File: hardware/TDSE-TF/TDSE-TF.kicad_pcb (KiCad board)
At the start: 2 copper layers, 153.2 x 91.6 mm, 37 parts, among them J1 Nivel de agua, J10 CN10, J2 Tira LED, J3 +5VCC entrada, J5 Bomba, J6 Nivel de luz, J7 CN7, J8 Humedad de suelo, J9 Conector LCD16x02, Q1 IRLZ44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

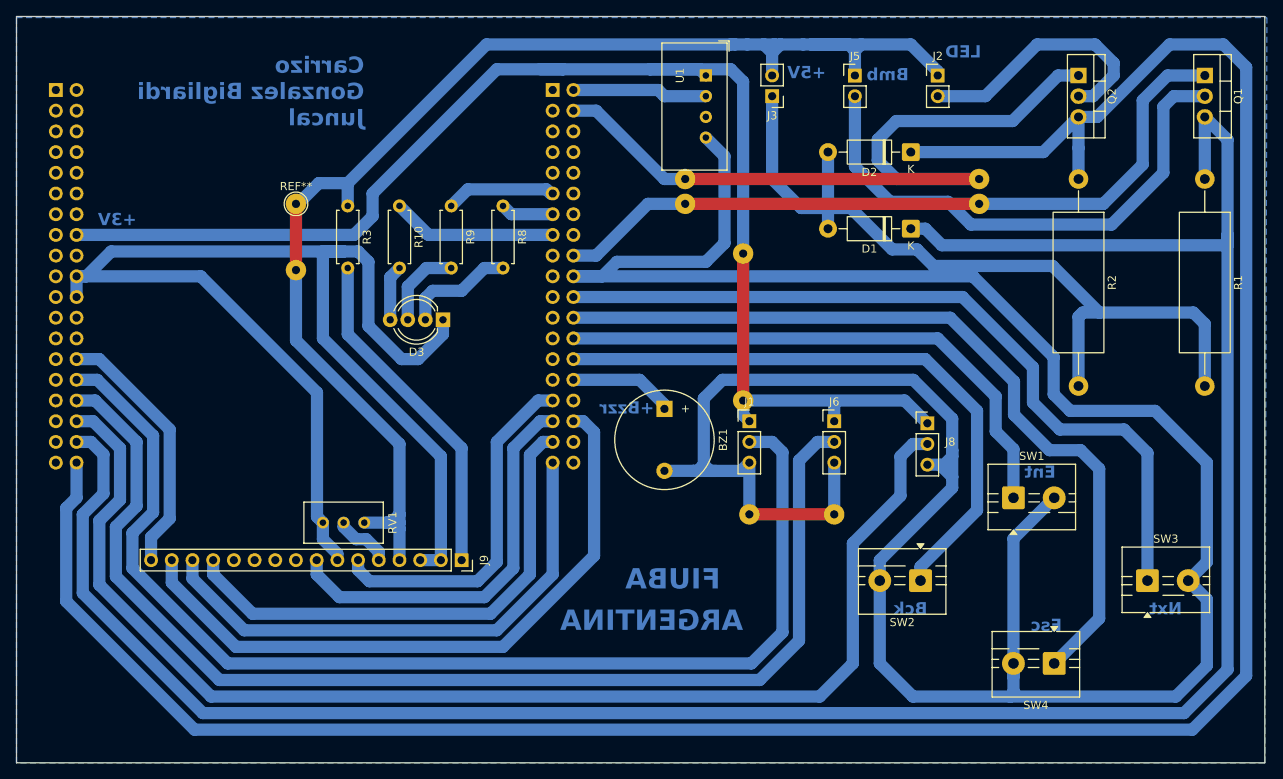
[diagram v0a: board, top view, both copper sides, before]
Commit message: Circuito final - Rev2
Revisión 2 del circuito esquemático y del PCB.
Cambios en conexiones del LCD.
Ajustes de Capa FFab.
Adjunto nota sobre configuración de jumpres y orden de conexionado de la placa.
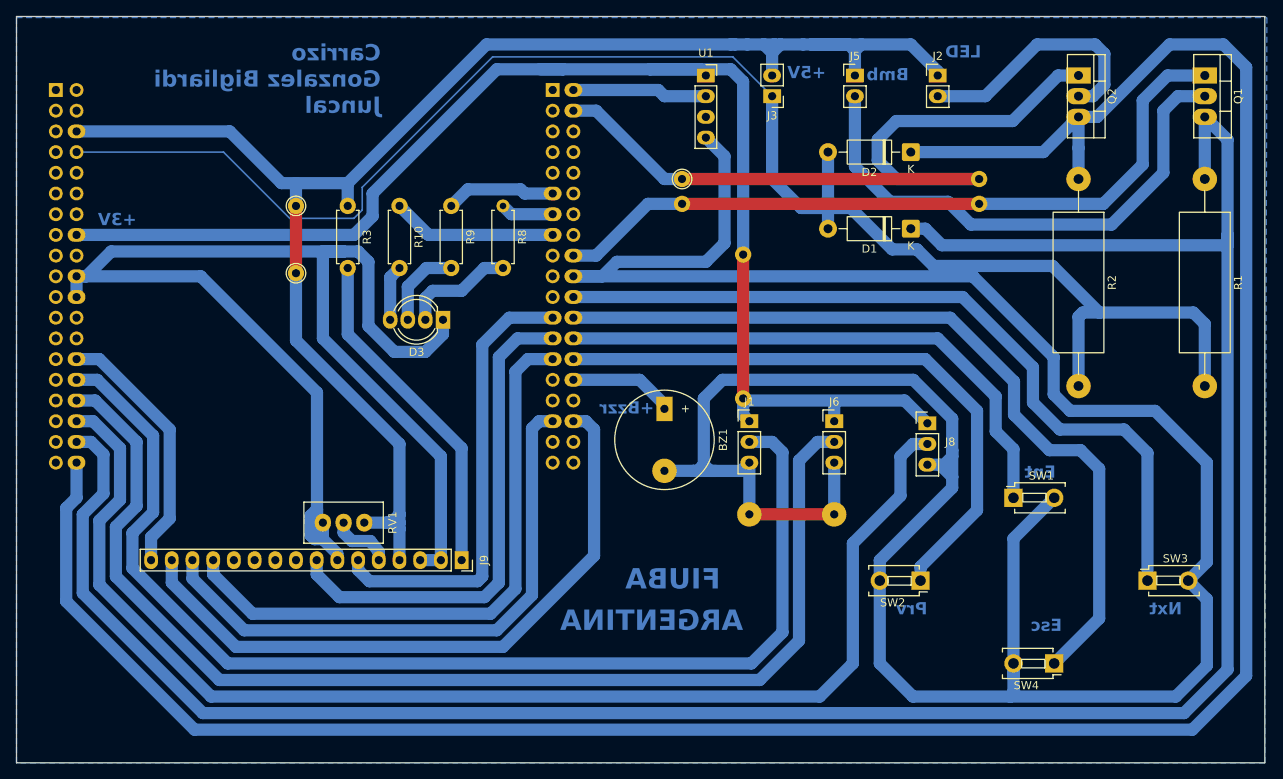
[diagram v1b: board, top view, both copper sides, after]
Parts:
- removed the ? at (212.6, 61.0)
- removed the ? at (212.6, 42.9)
- removed the ? at (205.5, 36.8)
- removed the ? at (157.7, 45.0)
- removed the ? at (205.5, 33.8)
- removed the REF** at (157.7, 36.8)
- added ?: , , F.Cu at (205.1, 36.8)
- added ?: , , F.Cu at (212.6, 43.1)
- added ?: , , F.Cu at (212.6, 60.7)
- added REF**: TestPoint_THTPad_D2.0mm_Drill1.0mm, TestPoint:TestPoint_THTPad_D2.0mm_Drill1.0mm, F.Cu at (157.7, 37.1)
- added REF**: TestPoint_THTPad_D2.0mm_Drill1.0mm, TestPoint:TestPoint_THTPad_D2.0mm_Drill1.0mm, F.Cu at (157.7, 45.3)
- added REF**: TestPoint_THTPad_D2.0mm_Drill1.0mm, TestPoint:TestPoint_THTPad_D2.0mm_Drill1.0mm, F.Cu at (205.1, 33.8)
- R1: value 10R 2W -> 10 2W
- SW1, SW2, SW3, SW4: footprint TerminalBlock:TerminalBlock_MaiXu_MX126-5.0-02P_1x02_P5.00mm -> Button_Switch_THT:SW_PUSH_1P1T 2 pines
- U1: footprint Sensor:ASAIR_AM2302_P2.54mm_Vertical -> Connector_PinSocket_2.54mm:PinSocket_1x04_P2.54mm_Vertical
- turned U1 to 0 degrees
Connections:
- net /D6 renamed /LCD_D6
- net /D7 renamed /LCD_D7
- J10 pad 23: unconnected-(J10-Pin_23-Pad23) -> /LCD_RS
- J10 pad 25: unconnected-(J10-Pin_25-Pad25) -> /LCD_E
- J10 pad 27: unconnected-(J10-Pin_27-Pad27) -> /LCD_D4
- J10 pad 31: /RS -> unconnected-(J10-Pin_31-Pad31)
- J10 pad 33: /E -> /LCD_D5
- J10 pad 35: /D4 -> unconnected-(J10-Pin_35-Pad35)
- J10 pad 37: /D5 -> unconnected-(J10-Pin_37-Pad37)
- J7 pad 6: unconnected-(J7-Pin_6-Pad6) -> VCC
- J9 pad 13: /D4 -> /LCD_D4
- J9 pad 14: /D5 -> /LCD_D5
- J9 pad 6: /RS -> /LCD_RS
- J9 pad 8: /E -> /LCD_E
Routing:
- net GND: track 607.5 -> 716.5 mm
- net /LCD_D4: track 0.00 -> 74.0 mm
- net /LCD_D5: track 0.00 -> 71.7 mm
- net /D5: track 65.6 -> 0.00 mm
- net /D4: track 62.7 -> 0.00 mm
- net /LCD_E: track 0.00 -> 60.8 mm
- net /LCD_RS: track 0.00 -> 55.7 mm
- net /E: track 49.0 -> 0.00 mm
- net /RS: track 43.5 -> 0.00 mm
- net VCC: track 165.0 -> 196.2 mm
- net Net-(J2-Pin_2): track 32.1 -> 31.1 mm
- net Net-(J9-Pin_5): track 7.12 -> 7.64 mm
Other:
- board text added: "+3,3"
- board text added: "DATA"
- board text added: "Prv"
- board text removed: "Bck"

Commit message: PCB final Rev 2
Corregido conexionado de LCD.
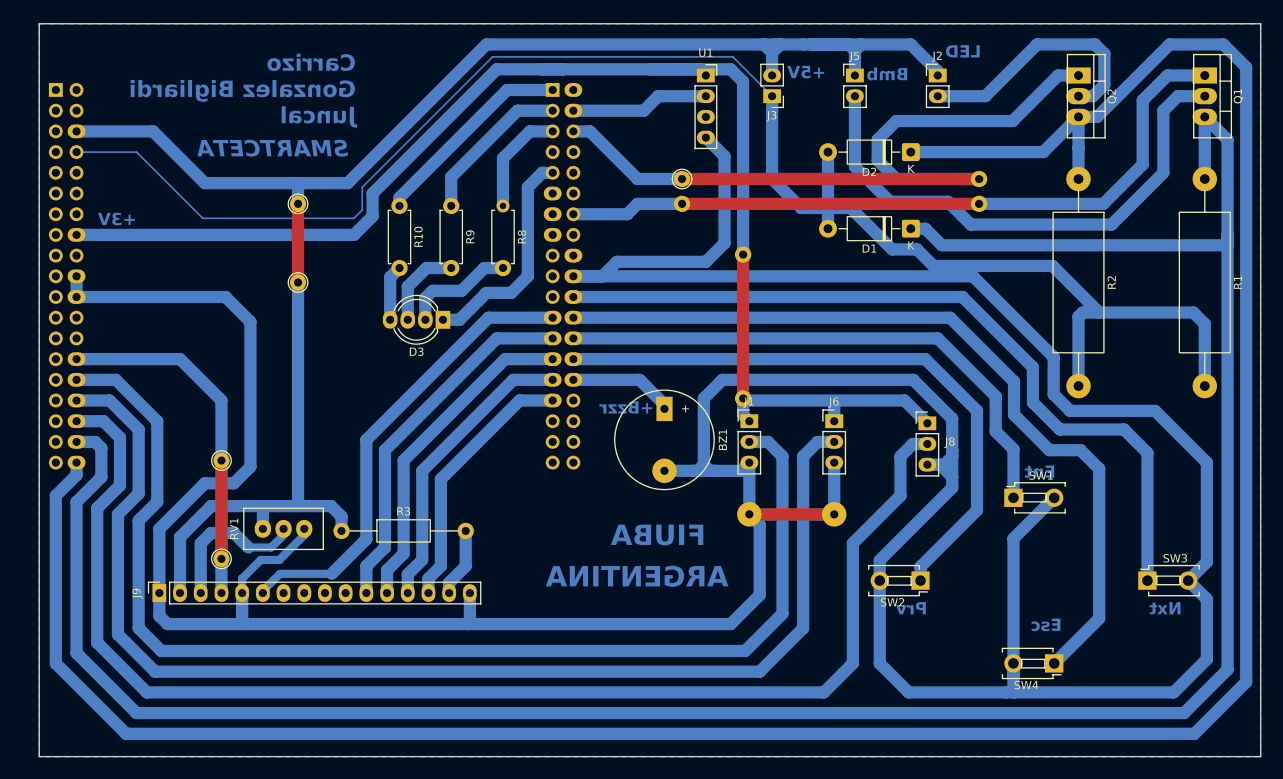
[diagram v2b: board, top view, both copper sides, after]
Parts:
- added REF**: TestPoint_THTPad_D2.0mm_Drill1.0mm, TestPoint:TestPoint_THTPad_D2.0mm_Drill1.0mm, F.Cu at (158.0, 36.8)
- added REF**: TestPoint_THTPad_D2.0mm_Drill1.0mm, TestPoint:TestPoint_THTPad_D2.0mm_Drill1.0mm, F.Cu at (158.0, 46.5)
- J1: value Nivel de agua -> Sensor nivel de agua
- J6: value Nivel de luz -> Sensor nivel de luz
- J8: value Humedad de suelo -> Sensor humedad de suelo
- R3: footprint Resistor_THT:R_Axial_DIN0207_L6.3mm_D2.5mm_P7.62mm_Horizontal -> Resistor_THT:R_Axial_DIN0207_L6.3mm_D2.5mm_P15.24mm_Horizontal
- U1: value DHT22 -> AM2302
- moved R3 39.9 mm to (163.3, 77.0), turned to 0 degrees
- moved J9 37.3 mm to (141.0, 84.6), turned to 90 degrees
- moved REF** 36.2 mm to (148.6, 80.4)
- moved REF** 32.6 mm to (148.6, 68.3), turned to 90 degrees
- moved RV1 12.5 mm to (153.7, 76.7), turned to 90 degrees
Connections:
- J10 pad 1: unconnected-(J10-Pin_1-Pad1) -> /LED Azul
- J10 pad 11: /LED Verde -> unconnected-(J10-Pin_11-Pad11)
- J10 pad 13: /LED Rojo -> unconnected-(J10-Pin_13-Pad13)
- J10 pad 14: unconnected-(J10-Pin_14-Pad14) -> /Driver Bomba
- J10 pad 15: /LED Azul -> unconnected-(J10-Pin_15-Pad15)
- J10 pad 18: /Driver Bomba -> unconnected-(J10-Pin_18-Pad18)
- J10 pad 2: /Medicion DHT22 (AM2302) -> unconnected-(J10-Pin_2-Pad2)
- J10 pad 23: /LCD_RS -> /LCD_E
- J10 pad 25: /LCD_E -> /LCD_D4
- J10 pad 27: /LCD_D4 -> /LCD_D5
- J10 pad 29: unconnected-(J10-Pin_29-Pad29) -> /LCD_D6
- J10 pad 3: unconnected-(J10-Pin_3-Pad3) -> /LED Verde
- J10 pad 31: unconnected-(J10-Pin_31-Pad31) -> /LCD_D7
- J10 pad 33: /LCD_D5 -> unconnected-(J10-Pin_33-Pad33)
- J10 pad 34: /LCD_D6 -> unconnected-(J10-Pin_34-Pad34)
- J10 pad 4: /Driver Tira LED -> /Medicion DHT22 (AM2302)
- J10 pad 5: unconnected-(J10-Pin_5-Pad5) -> /LED Rojo
- J10 pad 6: unconnected-(J10-Pin_6-Pad6) -> /Driver Tira LED
- J7 pad 28: /LCD_D7 -> /LCD_RS
- J9 pad 1: Net-(J9-Pin_1) -> GND
- J9 pad 11: unconnected-(J9-Pin_11-Pad11) -> /LCD_D4
- J9 pad 12: unconnected-(J9-Pin_12-Pad12) -> /LCD_D5
- J9 pad 13: /LCD_D4 -> /LCD_D6
- J9 pad 14: /LCD_D5 -> /LCD_D7
- J9 pad 15: /LCD_D6 -> /LCD_A
- J9 pad 16: /LCD_D7 -> GND
- J9 pad 2: GND -> VCC
- J9 pad 3: GND -> /LCD_Vo
- J9 pad 4: VCC -> /LCD_RS
- J9 pad 5: Net-(J9-Pin_5) -> GND
- J9 pad 6: /LCD_RS -> /LCD_E
- J9 pad 7: GND -> unconnected-(J9-Pin_7-Pad7)
- J9 pad 8: /LCD_E -> unconnected-(J9-Pin_8-Pad8)
- R3 pad 2: Net-(J9-Pin_1) -> /LCD_A
- REF** pad 1: VCC -> /LCD_RS
- REF** pad 2: (no net) -> /LCD_RS
- RV1 pad 2: Net-(J9-Pin_5) -> /LCD_Vo
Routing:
- net /LCD_D6: track 80.9 -> 36.4 mm
- net Net-(J9-Pin_1): track 40.8 -> 0.00 mm
- net /LCD_D5: track 71.7 -> 40.5 mm
- net /LCD_D4: track 74.0 -> 44.7 mm
- net GND: track 716.5 -> 739.9 mm
- net /LCD_Vo: track 0.00 -> 18.9 mm
- net /LCD_RS: track 55.7 -> 43.5 mm
- net VCC: track 196.2 -> 206.9 mm
- net /LCD_A: track 0.00 -> 8.46 mm
- net Net-(J9-Pin_5): track 7.64 -> 0.00 mm
- net /Medicion corriente tira LED: track 301.7 -> 308.8 mm
- net /LED Rojo: track 6.52 -> 13.3 mm
- net /LED Verde: track 13.5 -> 19.4 mm
- net /Medicion corriente bomba: track 288.1 -> 293.6 mm
- net /LED Azul: track 20.3 -> 25.3 mm
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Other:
- board size 153.2 x 91.6 mm -> 149.9 x 89.9 mm
- board text added: "0 5 Vo RS 0 E"
- board text added: "B G R"
- board text added: "D4 D5 D6 D7 A K"
- board text added: "SMARTCETA"
- board text removed: "D7 D6 D5 D4"
- board text removed: "E 0 RS Vo 5 0 0 5"

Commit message: PCB final Rev 3
Mejorados detalles del PCB y serigrafía
Añadida opcion de agregar un pullup para el dht22
Modificado el .ioc
Creado task_state_led.h (no terminado)
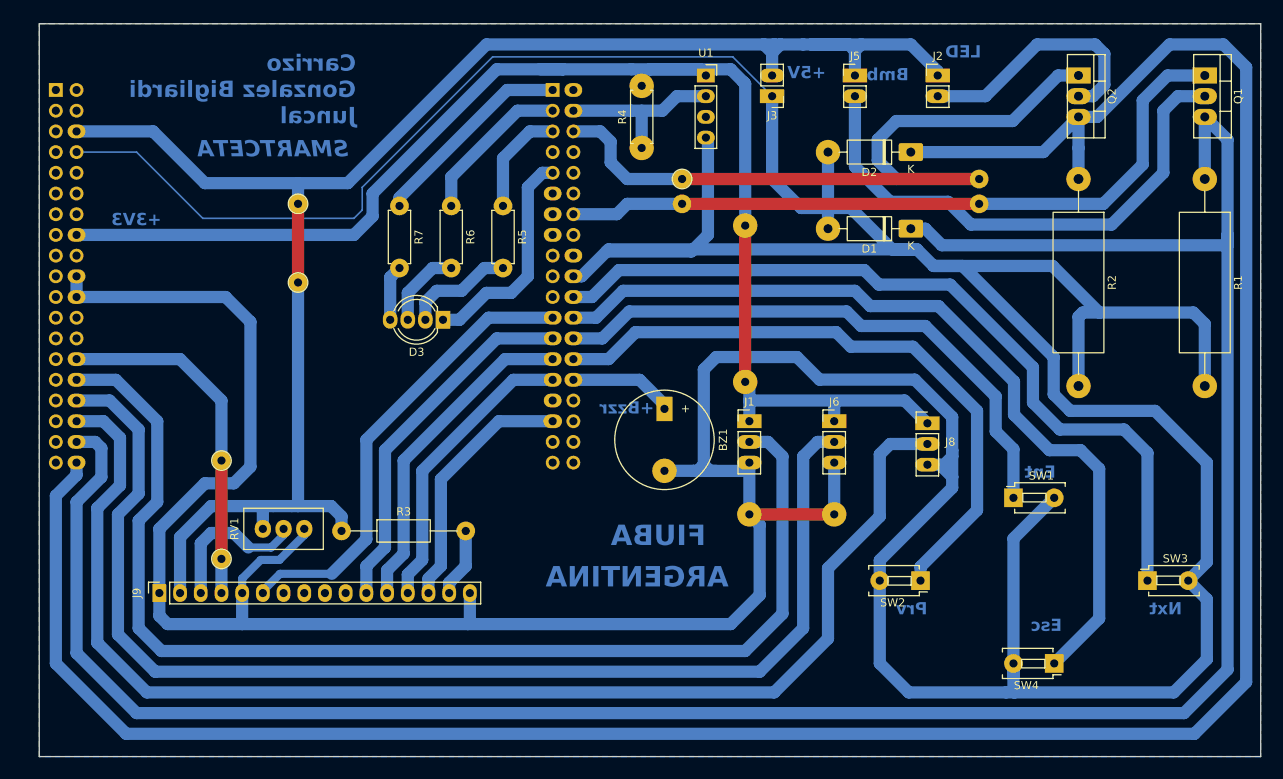
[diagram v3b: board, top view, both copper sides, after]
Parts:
- added R4: 5k1, Resistor_THT:R_Axial_DIN0207_L6.3mm_D2.5mm_P7.62mm_Horizontal, F.Cu at (200.2, 30.0)
- U1: value AM2302 -> DHT22
- moved ? 3.57 mm to (212.9, 39.5)
- moved ? 2.05 mm to (212.9, 58.7)
- renumbered R8 to R5, R9 to R6, R10 to R7
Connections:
- J10 pad 31: /LCD_D7 -> unconnected-(J10-Pin_31-Pad31)
- J10 pad 33: unconnected-(J10-Pin_33-Pad33) -> /LCD_D7
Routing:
- net /Medicion DHT22 (AM2302): track 17.0 -> 21.6 mm
- net GND: track 739.9 -> 735.5 mm
- net /Boton Siguiente: track 96.6 -> 99.3 mm
- net /Boton Enter: track 68.1 -> 70.8 mm
- net /Boton Anterior: track 75.9 -> 78.6 mm
- net /Boton Escape: track 100.7 -> 103.5 mm
- net /Medicion nivel de humedad: track 160.9 -> 159.0 mm
- net /+3.3V: track 170.6 -> 172.1 mm
- net /Driver Tira LED: track 95.9 -> 97.4 mm
- net /LCD_D7: track 32.3 -> 31.3 mm
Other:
- board text added: "+3V3"
- board text removed: "+3,3"
- board text removed: "+3V"

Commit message: PCB final Rev 4 y agregado led de estado RGB
Agregó la lógica de LED RGB de estado con PWM
Se mejoró el PCB y se incorporaron fichas de conexión mejores para alimentacion y cargas
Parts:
- J2, J3, J5: footprint Connector_PinHeader_2.54mm:PinHeader_1x02_P2.54mm_Vertical -> Connector_JST:JST_EH_B2B-EH-A_1x02_P2.50mm_Vertical
- moved J2 0.26 mm to (236.7, 21.1), turned to -90 degrees
- turned J3 to 90 degrees
- turned J5 to -90 degrees
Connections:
- J10 pad 1: /LED Azul -> unconnected-(J10-Pin_1-Pad1)
- J10 pad 17: unconnected-(J10-Pin_17-Pad17) -> /LED Azul
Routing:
- net GND: track 735.5 -> 768.4 mm
- net /LED Azul: track 25.3 -> 21.3 mm
- net /+3.3V: track 172.1 -> 170.8 mm
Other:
- board text added: "Rev 4"

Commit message: PCB final Rev 5 y buzzer
Se añadió la funcionalidad de buzzer al código
Se añadió un transistor como driver par el buzzer
Se actualizó el PCB
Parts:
- added ?: , , F.Cu at (163.3, 72.9)
- added Q3: MPSA42, Package_TO_SOT_THT:TO-92_Inline, F.Cu at (204.5, 55.1)
- added R8: 3k3, Resistor_THT:R_Axial_DIN0207_L6.3mm_D2.5mm_P7.62mm_Horizontal, F.Cu at (199.1, 58.4)
- added REF**: TestPoint_THTPad_D2.0mm_Drill1.0mm, TestPoint:TestPoint_THTPad_D2.0mm_Drill1.0mm, F.Cu at (178.6, 72.9)
- moved BZ1 12.9 mm to (198.6, 74.2), turned to 0 degrees
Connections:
- BZ1 pad 1: /Buzzer -> VCC
- BZ1 pad 2: GND -> Net-(BZ1--)
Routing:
- net VCC: track 206.9 -> 244.8 mm
- net Net-(BZ1--): track 0.00 -> 17.2 mm
- net Net-(Q3-B): track 0.00 -> 13.1 mm
- net /Buzzer: track 13.0 -> 7.37 mm
- net GND: track 768.4 -> 770.9 mm
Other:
- board text added: "Rev 5"
- board text added: "e b c"
- board text removed: "+Bzzr"
- board text removed: "Rev 4"

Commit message: PCB final Rev 6
Se añadió compatibilidad con botones de 4 patitas
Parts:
- added REF**: SW_PUSH_6mm, Button_Switch_THT:SW_PUSH_6mm, F.Cu at (250.5, 69.6)
- added REF**: SW_PUSH_6mm, Button_Switch_THT:SW_PUSH_6mm, F.Cu at (234.1, 79.8)
- added REF**: SW_PUSH_6mm, Button_Switch_THT:SW_PUSH_6mm, F.Cu at (267.0, 79.8)
- added REF**: SW_PUSH_6mm, Button_Switch_THT:SW_PUSH_6mm, F.Cu at (250.5, 88.3)
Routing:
- net /Boton Siguiente: track 99.3 -> 105.8 mm
- net /Boton Enter: track 70.8 -> 77.3 mm
- net /Boton Anterior: track 78.6 -> 82.0 mm
- net /Boton Escape: track 103.5 -> 105.2 mm
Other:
- board text added: "Rev 6"
- board text removed: "Rev 5"

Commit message: Finalizado modo falla y actualizacion de PCB
Se terminó el modo falla
Se ajustaron tamaños y ubicaciones de etiquetas para el FFab del PCB y se corrigió la ubicacion del DHT22
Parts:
- J1: value Sensor nivel de agua -> Sensor agua
- J3: value +5VCC entrada -> +5VCC
- J6: value Sensor nivel de luz -> Sensor luz
- J8: value Sensor humedad de suelo -> Sensor humedad
